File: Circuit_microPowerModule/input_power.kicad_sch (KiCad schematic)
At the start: 5 parts, among them Q1 S8550, SW1 RotaryEncoder_Switch, U2 MAX485E

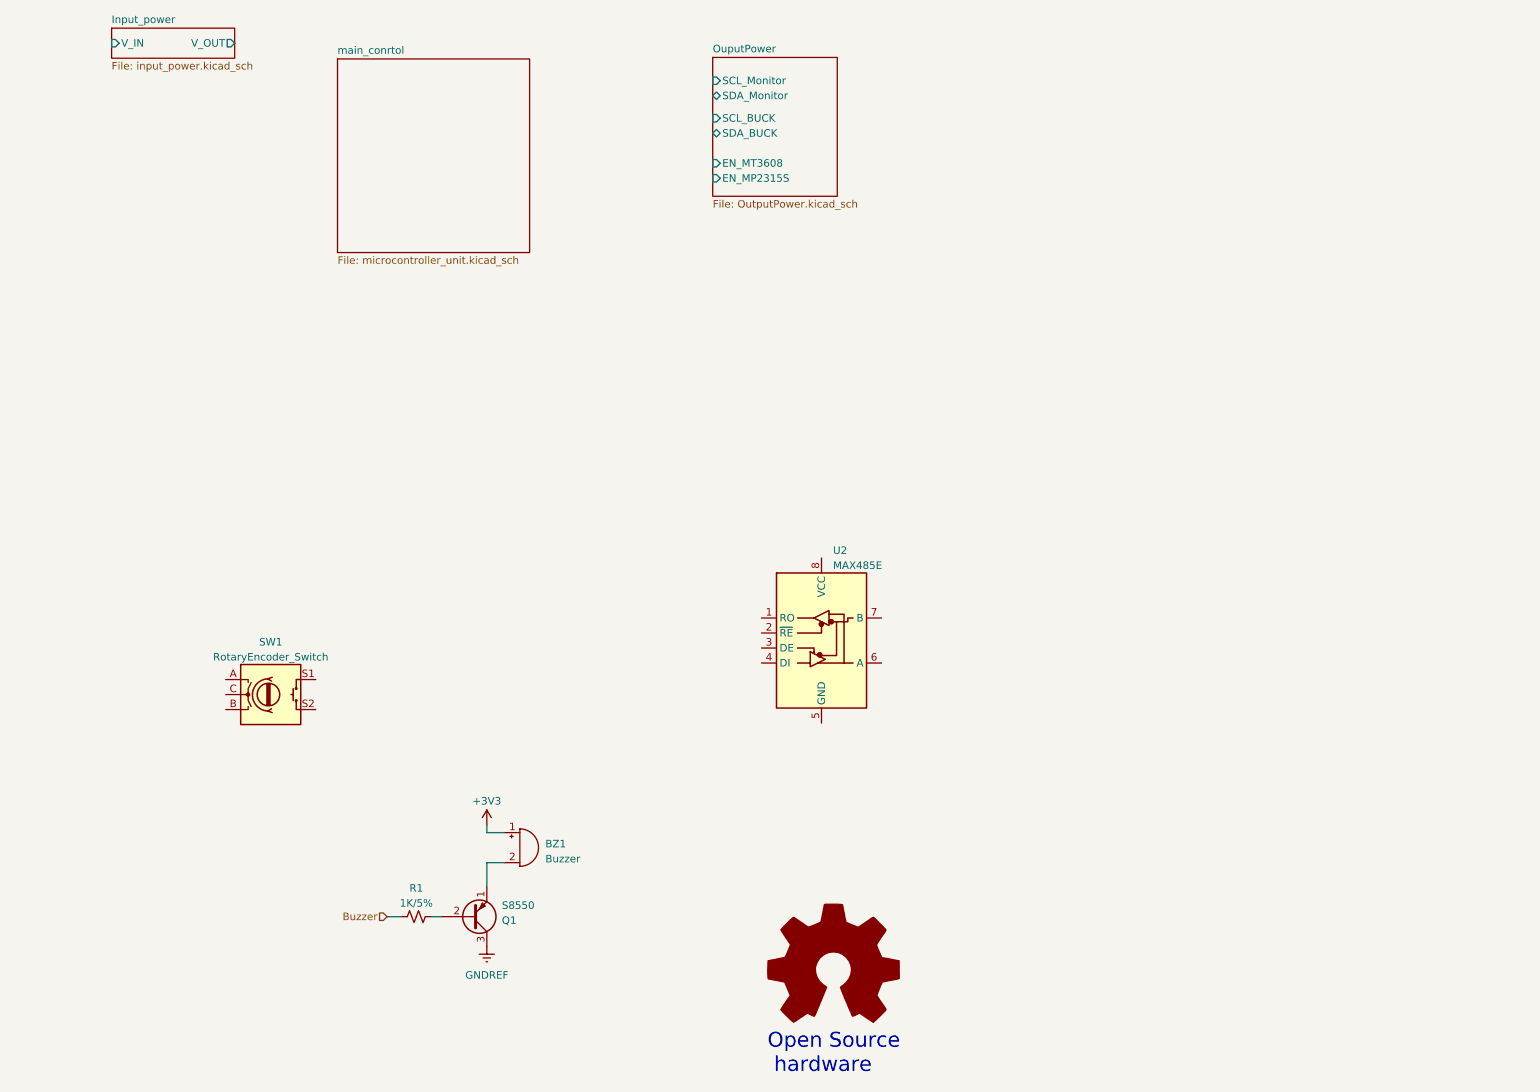
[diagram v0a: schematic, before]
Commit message: added input power OVP circuit
update buck-boost circuit
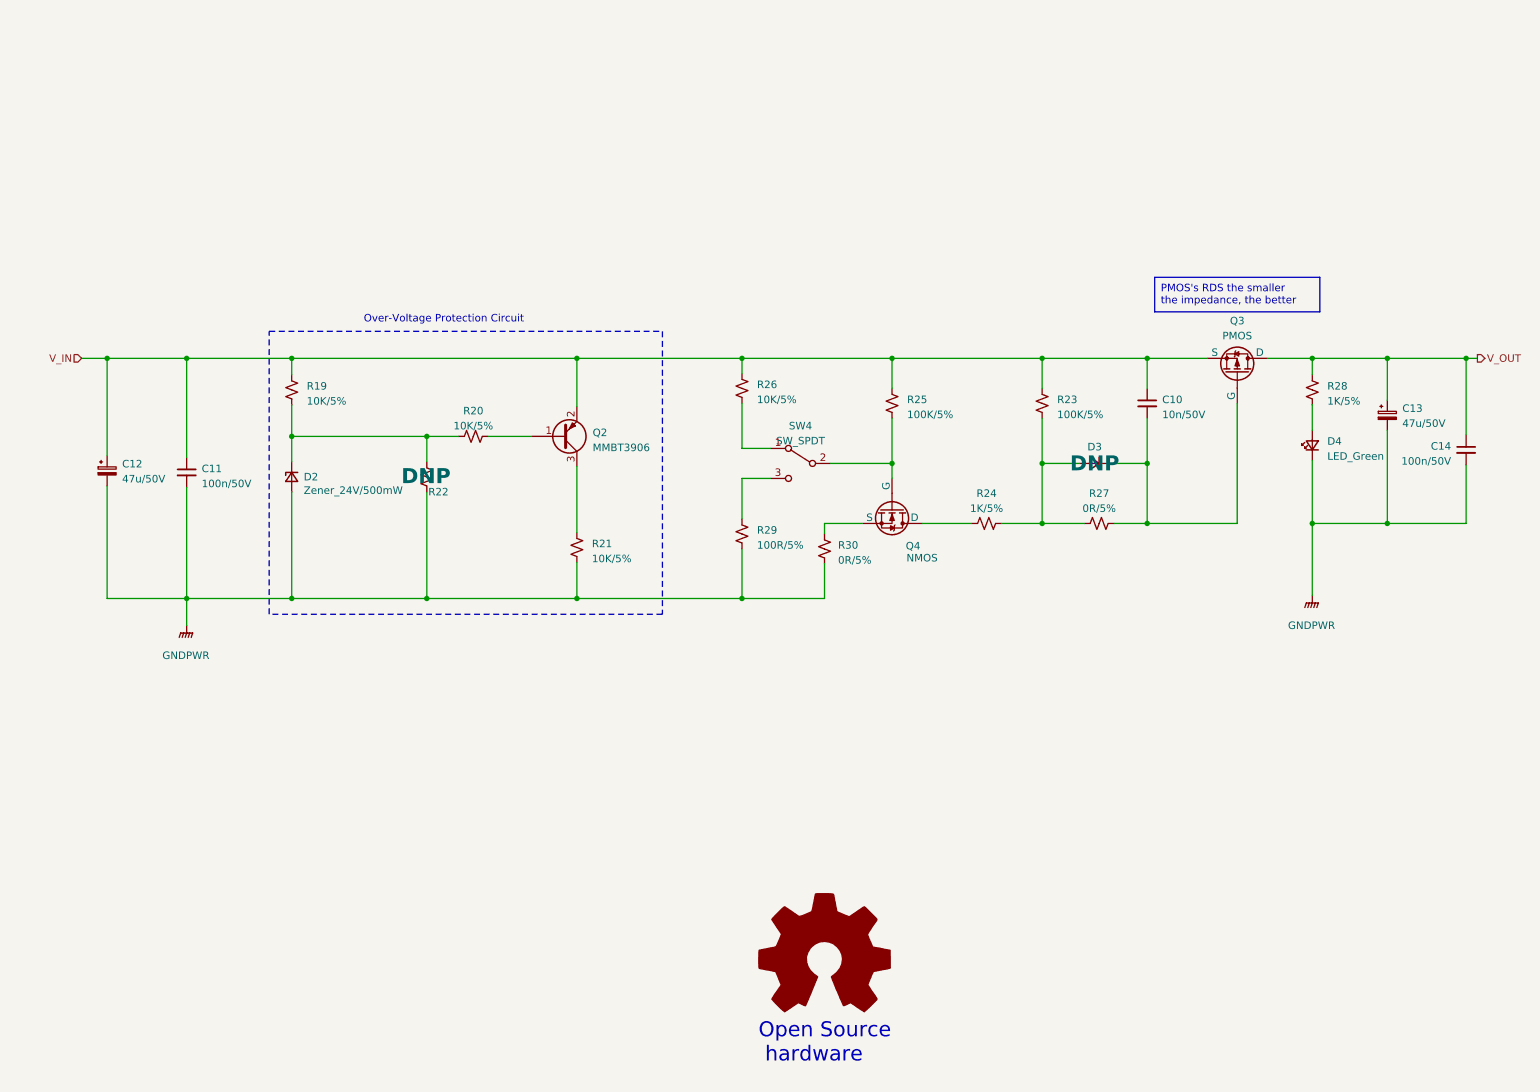
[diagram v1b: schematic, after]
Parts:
- removed BZ1: Buzzer, symbol Device:Buzzer
- removed Q1: S8550, Package_TO_SOT_THT:TO-92_Inline, symbol Transistor_BJT:S8550
- removed R1: 1K/5%, Resistor_SMD:R_0603_1608Metric, symbol Device:R_Small_US
- removed SW1: RotaryEncoder_Switch, symbol Device:RotaryEncoder_Switch
- removed U2: MAX485E, symbol Interface_UART:MAX485E
- added C10: 10n/50V, symbol Device:C_Small
- added C11, C14: 100n/50V, symbol Device:C_Small
- added C12, C13: 47u/50V, symbol Device:C_Polarized_Small
- added D2: Zener_24V/500mW, symbol Device:D_Zener_Small
- added D3: DNP, symbol Device:D_Small
- added D4: LED_Green, symbol Device:LED_Small
- added Q2: MMBT3906, Package_TO_SOT_SMD:SOT-23, symbol Transistor_BJT:MMBT3906
- added Q3: PMOS, symbol Simulation_SPICE:PMOS
- added Q4: NMOS, symbol Simulation_SPICE:NMOS
- added R19, R20, R21, R26: 10K/5%, symbol Device:R_Small_US
- added R22: DNP, symbol Device:R_Small_US
- added R23, R25: 100K/5%, symbol Device:R_Small_US
- added R24, R28: 1K/5%, symbol Device:R_Small_US
- added R27, R30: 0R/5%, symbol Device:R_Small_US
- added R29: 100R/5%, symbol Device:R_Small_US
- added SW4: SW_SPDT, symbol Switch:SW_SPDT
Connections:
- new net: D4.2 (A), R28.2
- new net: Q2.1 (B), R20.2
- new net: Q2.3 (C), R21.1
- new net: D2.1 (K), R19.2, R20.1, R22.1
- new net: D3.2 (A), R23.2, R24.2, R27.1
- new net: C10.2, D3.1 (K), Q3.2 (G), R27.2
- new net: R26.2, SW4.1 (A)
- new net: R29.1, SW4.3 (C)
- new net: Q4.1 (D), R24.1
- new net: Q4.2 (G), R25.2, SW4.2 (B)
- new net: Q4.3 (S), R30.2
- new net GNDPWR: C11.2, C12.2, C13.2, C14.2, D2.2 (A), D4.1 (K), R21.2, R22.2, R29.2, R30.1
- new net V_IN: C10.1, C11.1, C12.1, Q2.2 (E), Q3.3 (S), R19.1, R23.1, R25.1, R26.1
- new net V_OUT: C13.1, C14.1, Q3.1 (D), R28.1
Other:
- removed sheet Input_power
- removed sheet OuputPower
- removed sheet main_conrtol
- note added: "Over-Voltage Protection Circuit"
- title: µPower Module -> (none)

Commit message: added boost circuit
create peripheral schematic
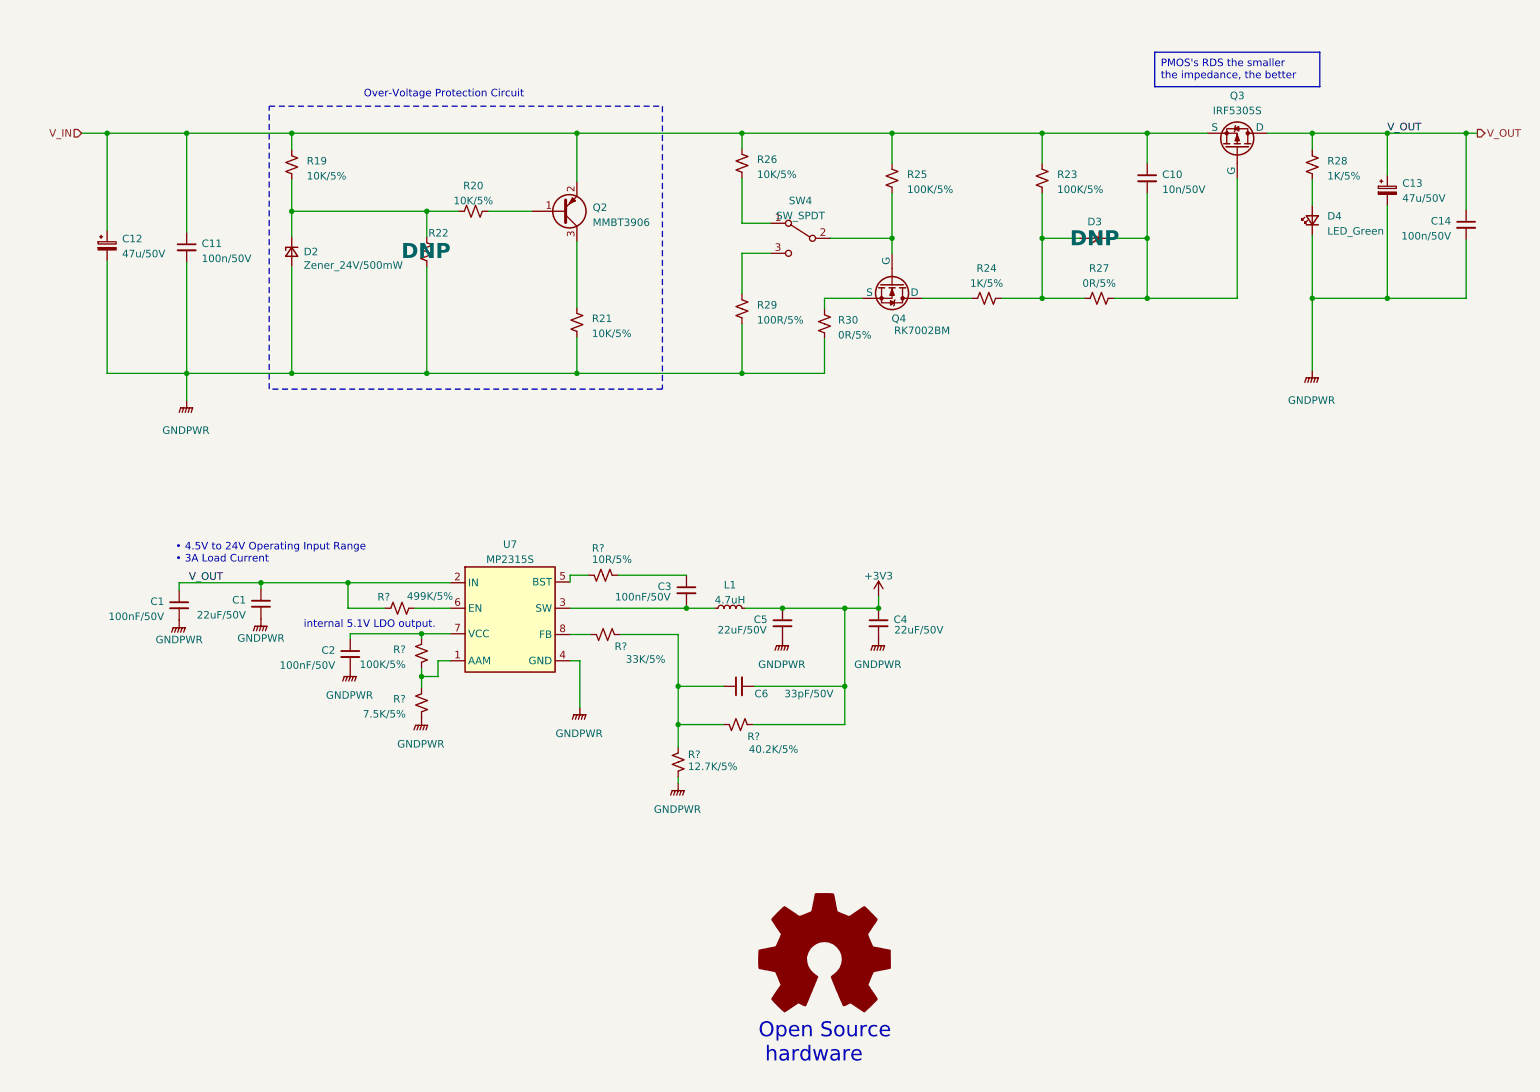
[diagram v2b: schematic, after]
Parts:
- added C1, C2, C3: 100nF/50V, symbol Device:C_Small
- added C1, C4, C5: 22uF/50V, symbol Device:C_Small
- added C6: 33pF/50V, symbol Device:C_Small
- added L1: 4.7uH, symbol Device:L_Small
- added R?: 10R/5%, Resistor_SMD:R_0603_1608Metric, symbol Device:R_Small_US
- added R?: 12.7K/5%, Resistor_SMD:R_0603_1608Metric, symbol Device:R_Small_US
- added R?: 7.5K/5%, Resistor_SMD:R_0603_1608Metric, symbol Device:R_Small_US
- added R?: 40.2K/5%, Resistor_SMD:R_0603_1608Metric, symbol Device:R_Small_US
- added R?: 100K/5%, Resistor_SMD:R_0603_1608Metric, symbol Device:R_Small_US
- added R?: 33K/5%, Resistor_SMD:R_0603_1608Metric, symbol Device:R_Small_US
- added R?: 499K/5%, Resistor_SMD:R_0603_1608Metric, symbol Device:R_Small_US
- added U7: MP2315S, Package_TO_SOT_SMD:TSOT-23-8, symbol micro-PowerModule:MP2315S
- Q3: value PMOS -> IRF5305S; footprint (none) -> Package_TO_SOT_SMD:TO-263-2
- Q4: value NMOS -> RK7002BM
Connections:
- net GNDPWR: now also C1.2, C1.2, C2.2, C4.2, C5.2, R?.1, R?.2, U7.4 (GND)
- net V_OUT: now also C1.1, C1.1, R?.2, U7.2 (IN)
- new net: C2.1, R?.2, U7.7 (VCC)
- new net: R?.1, U7.5 (BST)
- new net: C3.1, R?.2
- new net: C3.2, L1.1, U7.3 (SW)
- new net: C6.1, R?.1, R?.1, R?.2
- new net: R?.1, R?.2, U7.1 (AAM)
- new net: R?.1, U7.6 (EN)
- new net: R?.2, U7.8 (FB)
- new net +3V3: C4.1, C5.1, C6.2, L1.2, R?.1
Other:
- note added: "internal 5.1V LDO output."
- moved on the sheet: C10, C11, C12, C13, C14, D2, D3, D4, Q2, Q3, Q4, R19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

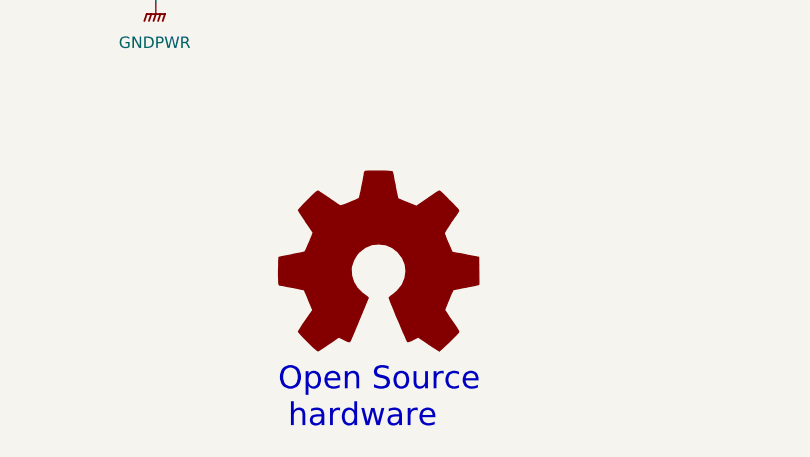
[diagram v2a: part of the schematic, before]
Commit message: added schematic svg file
added encoder wire, mikrobus connect
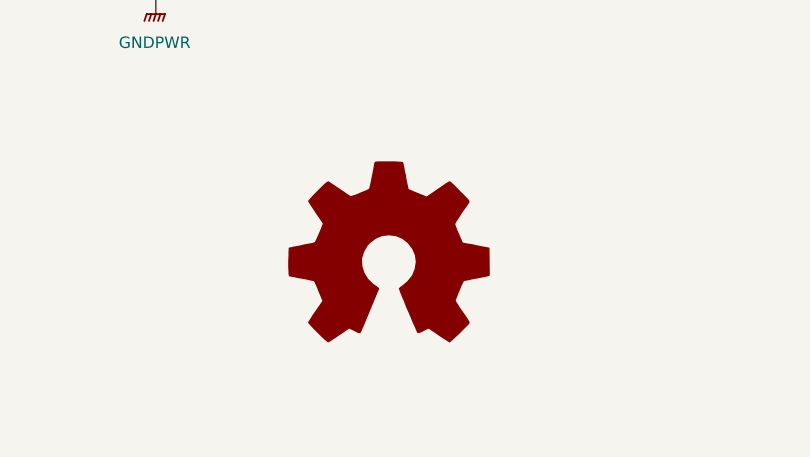
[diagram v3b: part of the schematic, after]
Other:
- note removed: "Open Source hardware"

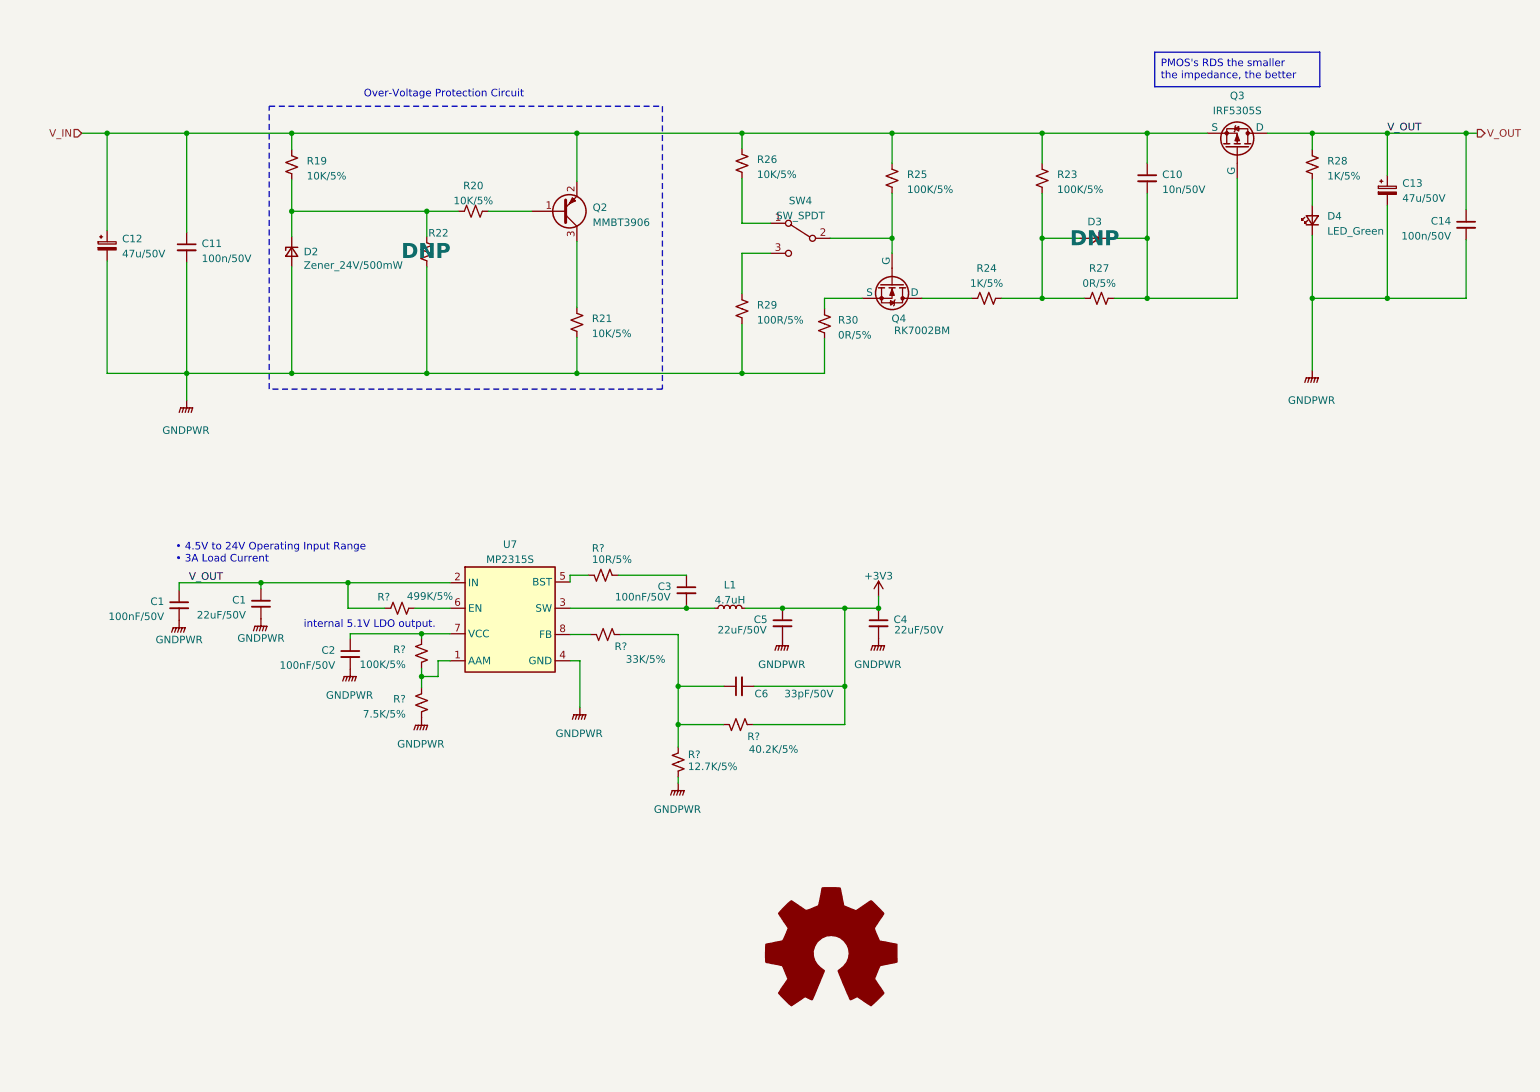
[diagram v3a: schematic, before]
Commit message: Completed microcontroller unit pin planning
update schematic
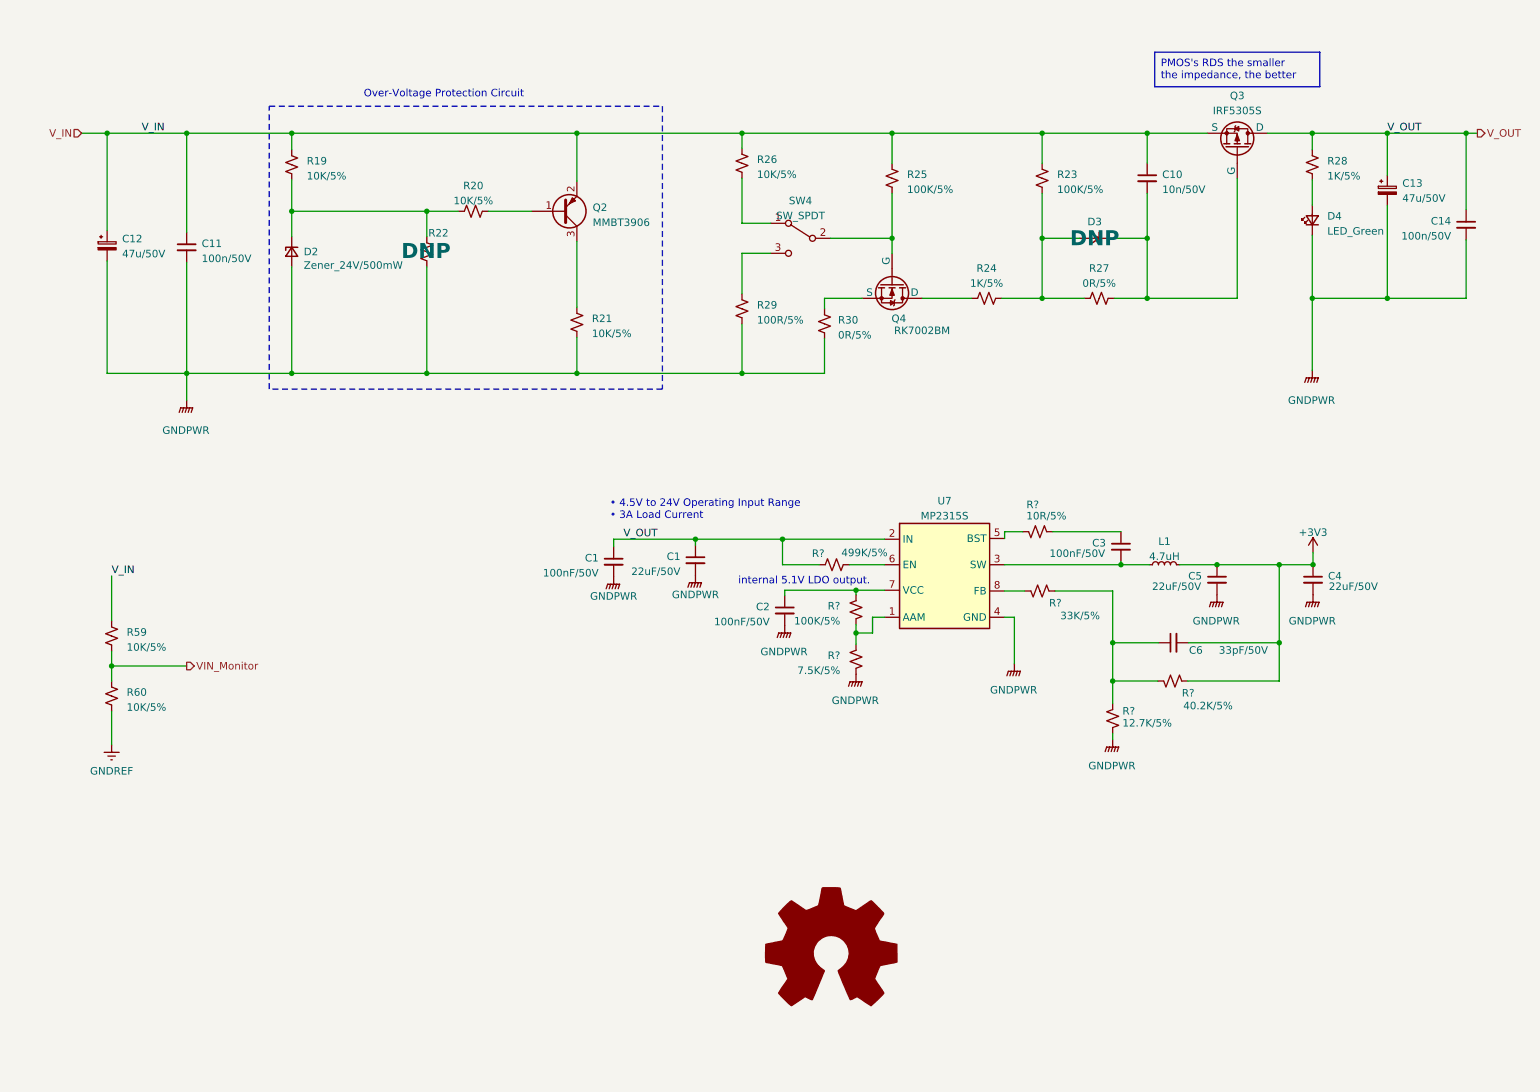
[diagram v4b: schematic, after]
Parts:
- added R59, R60: 10K/5%, symbol Device:R_Small_US
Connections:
- net V_IN: now also R59.1
- new net GNDREF: R60.2
- new net VIN_Monitor: R59.2, R60.1
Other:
- moved on the sheet: C1, C2, C3, C4, C5, C6, L1, R?, U7
